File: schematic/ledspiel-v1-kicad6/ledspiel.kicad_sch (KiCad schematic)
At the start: 148 parts, among them J1 Conn_01x16_Male, J2 SWD Debug, J3 USART Debug, J4 USB_B_Micro, J5 USB_C_Receptacle_USB2.0, J70 Micro_SD_Card_Det, J80 Conn_Battery, Q10 BSS138, Q11 BSS138, Q12 BSS138, Q13 BSS138, Q14 BSS138, Q60 SFH300-3/4, Q70 IRLML6402, Q80 BSS138, U1 STM32F405RGTx, U100 LM4861, U2 USBLC6-2SC6, U60 TSOP312xx, U80 MCP1640CH, U81 LP38693MP-3.3, Y1 8MHz, Y2 32768Hz

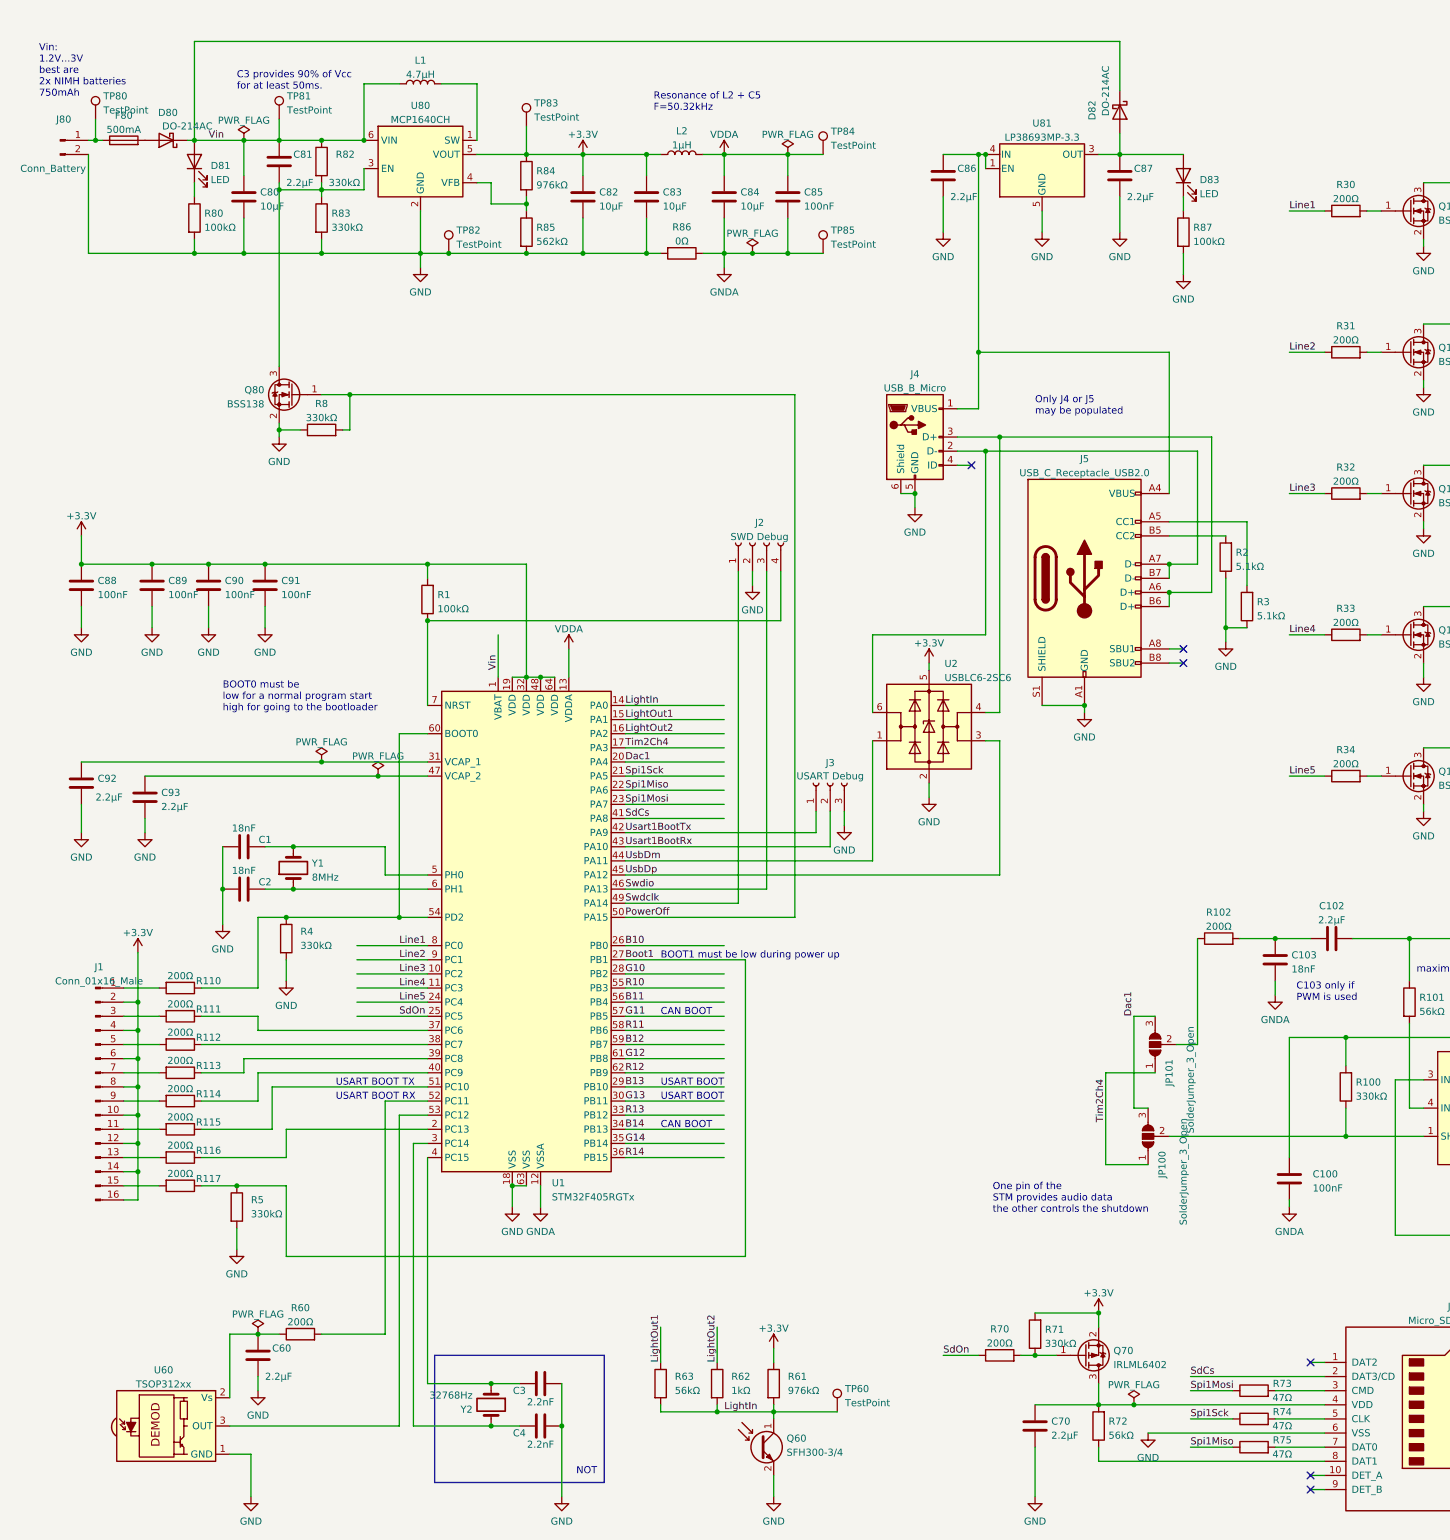
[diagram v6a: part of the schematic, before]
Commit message: WIP: Schematic should be somehow complete
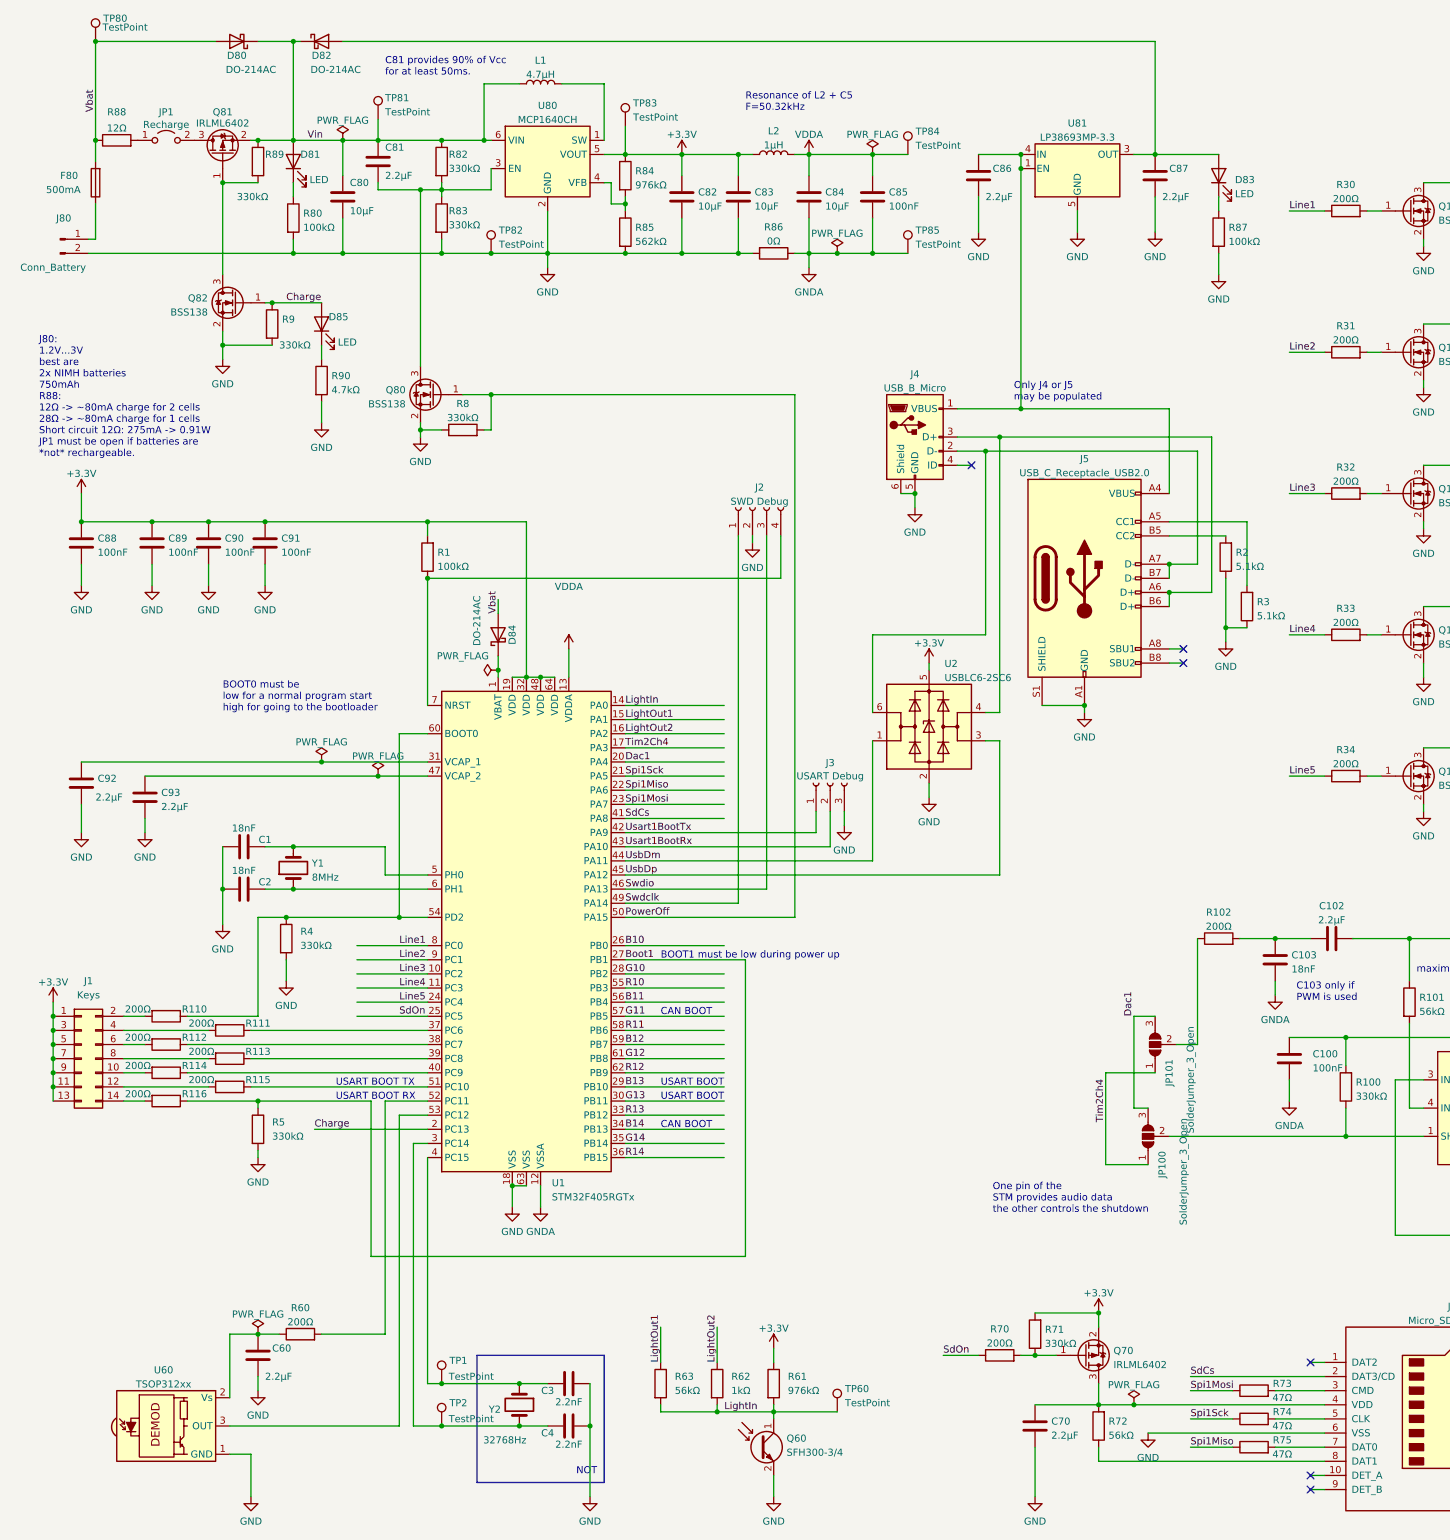
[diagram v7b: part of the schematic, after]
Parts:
- removed J1: Conn_01x16_Male, symbol Connector:Conn_01x16_Male
- removed R116: 200Ω, Resistor_SMD:R_0805_2012Metric_Pad1.20x1.40mm_HandSolder, symbol Device:R
- added D84: DO-214AC, symbol Device:D_Schottky
- added D85: LED, LED_SMD:LED_0805_2012Metric_Pad1.15x1.40mm_HandSolder, symbol Device:LED
- added J1: Keys, symbol Connector_Generic:Conn_02x07_Odd_Even
- added JP1: Recharge, symbol Jumper:Jumper_2_Open
- added Q81: IRLML6402, Package_TO_SOT_SMD:SOT-23, symbol Transistor_FET:IRLML6402
- added Q82: BSS138, Package_TO_SOT_SMD:SOT-23, symbol Transistor_FET:BSS138
- added R88: 12Ω, Resistor_SMD:R_0805_2012Metric_Pad1.20x1.40mm_HandSolder, symbol Device:R
- added R89, R9: 330kΩ, Resistor_SMD:R_0805_2012Metric_Pad1.20x1.40mm_HandSolder, symbol Device:R
- added R90: 4.7kΩ, Resistor_SMD:R_0805_2012Metric_Pad1.20x1.40mm_HandSolder, symbol Device:R
- added TP1, TP2: TestPoint, TestPoint:TestPoint_Bridge_Pitch2.0mm_Drill0.7mm, symbol Connector:TestPoint
- renumbered R117 to R116
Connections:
- net +3.3V: now also J1.1 (Pin_1), J1.11 (Pin_11), J1.13 (Pin_13), J1.3 (Pin_3), J1.5 (Pin_5), J1.7 (Pin_7), J1.9 (Pin_9)
- net GND: now also Q82.2 (S), R9.2, R90.2
- net Vin: now also Q81.2 (S), R89.1; no longer U1.1 (VBAT)
- net at C3.2, U1.4 (PC15), Y2.1: now also TP1.1
- net at R110.2: now also J1.2 (Pin_2)
- net at R115.2: now also J1.12 (Pin_12)
- net at R116.2: now also J1.14 (Pin_14)
- net at R111.2: now also J1.4 (Pin_4)
- net at R112.2: now also J1.6 (Pin_6)
- net at R113.2: now also J1.8 (Pin_8)
- net at R114.2: now also J1.10 (Pin_10)
- net at F80.1, J80.1 (Pin_1): no longer TP80.1
- net at C4.2, U1.3 (PC14), Y2.2: now also TP2.1
- net Vbat: now reaches D80.2 (A), F80.2
- net Vbat: now also TP80.1, D84.2 (A), R88.1
- net Charge: now reaches U1.2 (PC13)
- net Charge: now also D85.2 (A), Q82.1 (G), R9.1
- new net: Q81.1 (G), Q82.3 (D), R89.2
- new net: D85.1 (K), R90.1
- new net: JP1.1 (A), R88.2
- new net: D84.1 (K), U1.1 (VBAT)
- new net: JP1.2 (B), Q81.3 (D)
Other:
- note added: "C81 provides 90% of Vcc for at least 50ms."
- note added: "J80: 1.2V...3V best are 2x NIMH batteries 750mAh R88: 12Ω -> ~80mA charge for 2 cells 28Ω -> ~80mA charge for 1 cells Short circuit 12Ω: 275mA -> 0.91W JP1 must be open if batteries are *not* rechargeable."
- note removed: "C3 provides 90% of Vcc for at least 50ms."
- note removed: "Vin: 1.2V...3V best are 2x NIMH batteries 750mAh"
- moved on the sheet: C100, C3, C4, C80, C81, C82, C83, C84, C85, C86, C87, C88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

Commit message: WIP
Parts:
- D80, D82, D84: value DO-214AC -> SK14
- J1: footprint (none) -> Connector_PinHeader_2.54mm:PinHeader_2x07_P2.54mm_Vertical
- J3: footprint (none) -> Connector_PinSocket_2.54mm:PinSocket_1x03_P2.54mm_Vertical
- J80: value Conn_Battery -> Battery; footprint (none) -> Connector_PinHeader_2.54mm:PinHeader_1x02_P2.54mm_Vertical
- JP1: footprint (none) -> Connector_PinHeader_2.54mm:PinHeader_1x02_P2.54mm_Vertical
- JP100: value SolderJumper_3_Open -> AudioEnable
- JP101: value SolderJumper_3_Open -> AudioData
- L2: footprint (none) -> Inductor_SMD:L_1008_2520Metric_Pad1.43x2.20mm_HandSolder
- Q60: footprint (none) -> LED_THT:LED_D5.0mm_Clear
- R88: footprint Resistor_SMD:R_0805_2012Metric_Pad1.20x1.40mm_HandSolder -> Resistor_THT:R_Axial_DIN0414_L11.9mm_D4.5mm_P15.24mm_Horizontal
- RV100: footprint LED_SMD:LED_0805_2012Metric_Pad1.15x1.40mm_HandSolder -> Potentiometer_THT:Potentiometer_Piher_PT-6-H_Horizontal
- Y1: footprint (none) -> Crystal:Crystal_HC49-U_Vertical
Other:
- moved on the sheet: C80, C90, C91, D80, D81, D82, JP101, L1, R2, R3, R80, R89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
